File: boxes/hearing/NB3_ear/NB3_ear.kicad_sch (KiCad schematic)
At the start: 4 parts, among them J1 Conn_01x06_Male

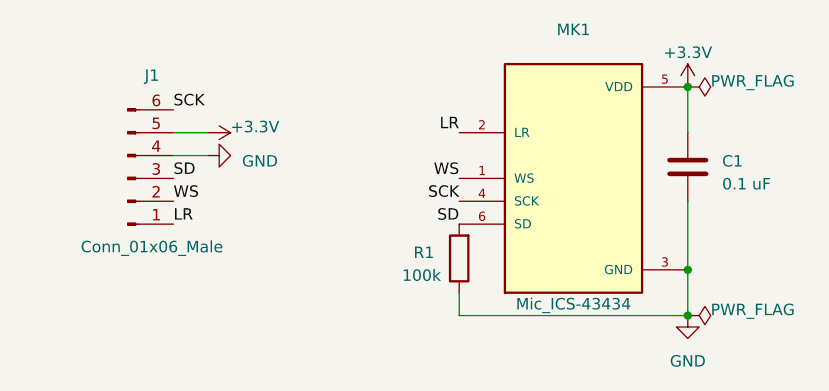
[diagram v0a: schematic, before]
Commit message: Added NB3 Ear PCB design
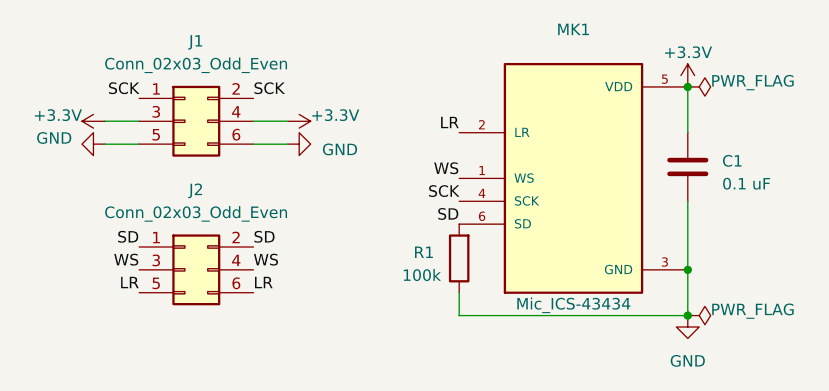
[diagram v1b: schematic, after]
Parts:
- removed J1: Conn_01x06_Male, Connector_PinHeader_2.54mm:PinHeader_1x06_P2.54mm_Horizontal, symbol Connector:Conn_01x06_Male
- added J1, J2: Conn_02x03_Odd_Even, Connector_PinHeader_2.54mm:PinHeader_2x03_P2.54mm_Vertical_SMD, symbol Connector_Generic:Conn_02x03_Odd_Even
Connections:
- net +3V3: now also J1.3 (Pin_3), J1.4 (Pin_4)
- net GND: now also J1.5 (Pin_5), J1.6 (Pin_6)
- net LR: now also J2.5 (Pin_5), J2.6 (Pin_6)
- net SCK: now also J1.1 (Pin_1), J1.2 (Pin_2)
- net SD: now also J2.1 (Pin_1), J2.2 (Pin_2)
- net WS: now also J2.3 (Pin_3), J2.4 (Pin_4)
